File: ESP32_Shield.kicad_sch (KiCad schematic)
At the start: 36 parts, among them J1 BME280, SHT40 Module, J10 SCD40 Module, J11 Conn_01x03, J12 Conn_01x03, J2 SCD40 Module, J3 Conn_01x02, J4 Qwiic_Vertical, J5 Conn_01x02, J6 Conn_01x02, J7 Conn_01x03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

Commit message: remove fix soldered tempertaure sesor
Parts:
- removed C6: 100n, Capacitor_SMD:C_0805_2012Metric, symbol Device:C
- removed U3: SHT40, PCM_SparkFun-Sensor:Sensirion_DFN-4_1.5x1.5mm_P0.8mm_SHT4x_NoCentralPad, symbol PCM_SparkFun-Sensor:SHT40
- added J13: SCD40 Module, PCM_SparkFun-Connector:1x04_P2.54mm, symbol PCM_SparkFun-Connector:Conn_01x04_P2.54mm
- added J14: BME280, SHT40 Module, PCM_SparkFun-Connector:1x04_P2.54mm, symbol PCM_SparkFun-Connector:Conn_01x04_P2.54mm
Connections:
- net +3V3: now also J13.2 (Pin_2), J14.1 (Pin_1)
- net GND: now also J13.1 (Pin_1), J14.2 (Pin_2)
- net SCK: now also J13.3 (Pin_3), J14.3 (Pin_3)
- net SDA: now also J13.4 (Pin_4), J14.4 (Pin_4)
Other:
- note removed: "SHT40 temperature and humidity"

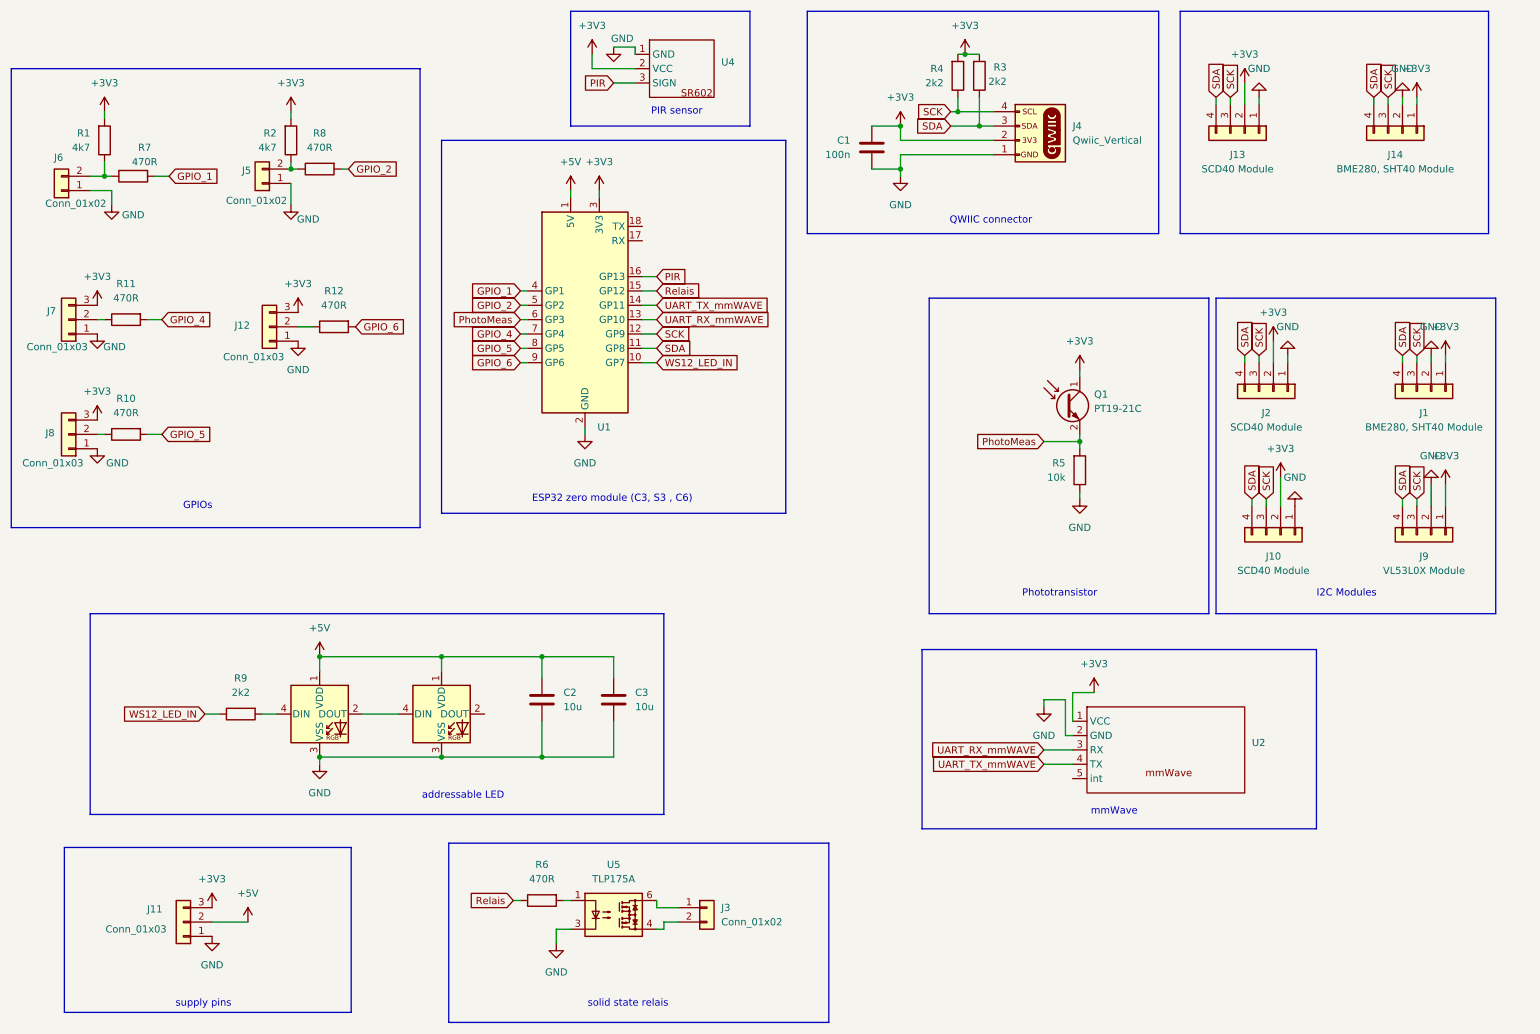
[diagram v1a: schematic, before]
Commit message: Feature/description on soldermask (#2)
* fix Readme

* enhance README with KiBOT usage instructions and asset generation workflow

* make shure everithing is english

* improve readme

* fix upload path

* fix tittle in readme

* add silk screen and mmWave connector

* Update artifact name in fabrication workflow

* try other pr pipeline

* add more JST connectors for UART

* add jst connector for aditional gpios
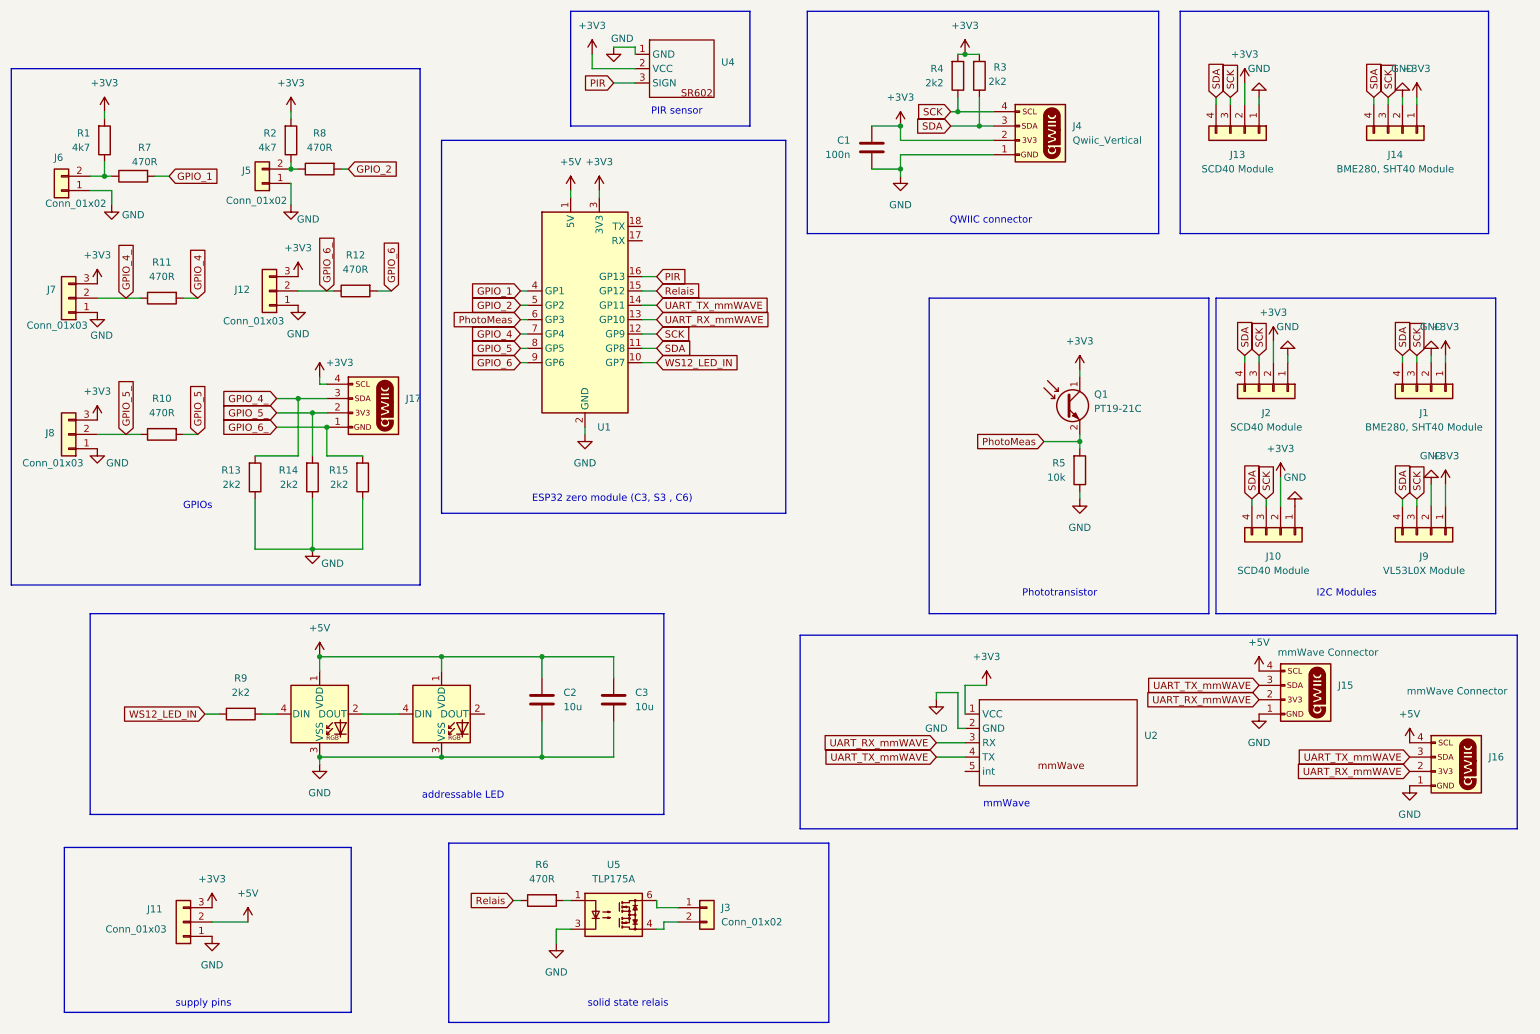
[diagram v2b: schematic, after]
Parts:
- added J15, J16, J17: mmWave Connector, PCM_SparkFun-Connector:JST_1x04_P1.0mm_Vertical_SMD, symbol PCM_SparkFun-Connector:Qwiic_Vertical
- added R13, R14, R15: 2k2, Resistor_SMD:R_0805_2012Metric, symbol Device:R
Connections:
- net +3V3: now also J17.4 (Pin_4)
- net +5V: now also J15.4 (Pin_4), J16.4 (Pin_4)
- net GND: now also J15.1 (Pin_1), J16.1 (Pin_1), R13.1, R14.1, R15.1
- net UART_RX_mmWAVE: now also J15.2 (Pin_2), J16.2 (Pin_2)
- net UART_TX_mmWAVE: now also J15.3 (Pin_3), J16.3 (Pin_3)
- net GPIO_6_: now reaches J12.2 (Pin_2), R12.1
- net GPIO_6_: now also J17.1 (Pin_1), R15.2
- net GPIO_5_: now reaches J8.2 (Pin_2), R10.1
- net GPIO_5_: now also J17.2 (Pin_2), R14.2
- net GPIO_4_: now reaches J7.2 (Pin_2), R11.1
- net GPIO_4_: now also J17.3 (Pin_3), R13.2
- new net: J15.NC1 (NC), J15.NC2 (NC)
- new net: J17.NC1 (NC), J17.NC2 (NC)
- new net: J16.NC1 (NC), J16.NC2 (NC)
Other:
- moved on the sheet: J12, J7, R10, R11, R12, U2
